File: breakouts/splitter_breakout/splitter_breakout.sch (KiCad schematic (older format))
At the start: 8 parts

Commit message: added breakout boards
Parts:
- removed H? (x4): MOUNTING_HOLE, symbol MOUNTING_HOLE
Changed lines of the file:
@@
 LIBS:scbd-16-63
 LIBS:tcm-63ax+
+LIBS:splitter_breakout-cache
 EELAYER 25 0
 EELAYER END
@@
 	8600 4200 9150 4200
 $Comp
-L MOUNTING_HOLE H?
-U 1 1 56A5DF97
-P 6300 2750
-F 0 "H?" H 6000 2800 60  0000 C CNN
-F 1 "MOUNTING_HOLE" H 6300 2900 60  0000 C CNN
-F 2 "" H 6300 2750 60  0000 C CNN
-F 3 "" H 6300 2750 60  0000 C CNN
-	1    6300 2750
-	1    0    0    -1
-$EndComp
-$Comp
-L MOUNTING_HOLE H?
-U 1 1 56A5DFB9
-P 6550 2750
-F 0 "H?" H 6250 2800 60  0000 C CNN
-F 1 "MOUNTING_HOLE" H 6550 2900 60  0000 C CNN
-F 2 "" H 6550 2750 60  0000 C CNN
-F 3 "" H 6550 2750 60  0000 C CNN
-	1    6550 2750
-	1    0    0    -1
-$EndComp
-$Comp
-L MOUNTING_HOLE H?
-U 1 1 56A5DFE1
-P 6800 2750
-F 0 "H?" H 6500 2800 60  0000 C CNN
-F 1 "MOUNTING_HOLE" H 6800 2900 60  0000 C CNN
-F 2 "" H 6800 2750 60  0000 C CNN
-F 3 "" H 6800 2750 60  0000 C CNN
-	1    6800 2750
-	1    0    0    -1
-$EndComp
-$Comp
-L MOUNTING_HOLE H?
-U 1 1 56A5E033
-P 7050 2750
-F 0 "H?" H 6750 2800 60  0000 C CNN
-F 1 "MOUNTING_HOLE" H 7050 2900 60  0000 C CNN
-F 2 "" H 7050 2750 60  0000 C CNN
-F 3 "" H 7050 2750 60  0000 C CNN
-	1    7050 2750
-	1    0    0    -1
-$EndComp
-$Comp
 L GND #PWR?

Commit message: work on breakouts
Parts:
- added U2: mounting_box, vna_footprints:POMONA_2400BOX, symbol mounting_box
- U1, U4, U5: renamed from U?; footprint (none) -> vna_footprints:732512200_SMA
- U3: renamed from U?; footprint (none) -> vna_footprints:FV1206
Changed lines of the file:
@@
 LIBS:scbd-16-63
 LIBS:tcm-63ax+
+LIBS:mounting_box
 LIBS:splitter_breakout-cache
 EELAYER 25 0
@@
 $EndDescr
 $Comp
-L PWR_SPLITTER U?
+L PWR_SPLITTER U3
 U 1 1 56A5DB75
 P 7650 3800
-F 0 "U?" H 7250 4200 60  0000 C CNN
+F 0 "U3" H 7250 4200 60  0000 C CNN
 F 1 "PWR_SPLITTER" H 7500 4300 60  0000 C CNN
-F 2 "" H 7650 3800 60  0000 C CNN
+F 2 "vna_footprints:FV1206" H 7650 3800 60  0001 C CNN
 F 3 "" H 7650 3800 60  0000 C CNN
 	1    7650 3800
@@
 $EndComp
 $Comp
-L CONN_SMA U?
+L CONN_SMA U5
 U 1 1 56A5DD34
 P 9700 4200
-F 0 "U?" H 9350 4400 60  0000 C CNN
+F 0 "U5" H 9350 4400 60  0000 C CNN
 F 1 "CONN_SMA" H 9550 4550 60  0000 C CNN
-F 2 "" H 9700 4200 60  0000 C CNN
+F 2 "vna_footprints:732512200_SMA" H 9700 4200 60  0001 C CNN
 F 3 "" H 9700 4200 60  0000 C CNN
 	1    9700 4200
@@
 $EndComp
 $Comp
-L CONN_SMA U?
+L CONN_SMA U4
 U 1 1 56A5DDCB
 P 9700 3350
-F 0 "U?" H 9350 3550 60  0000 C CNN
+F 0 "U4" H 9350 3550 60  0000 C CNN
 F 1 "CONN_SMA" H 9550 3700 60  0000 C CNN
-F 2 "" H 9700 3350 60  0000 C CNN
+F 2 "vna_footprints:732512200_SMA" H 9700 3350 60  0001 C CNN
 F 3 "" H 9700 3350 60  0000 C CNN
 	1    9700 3350
@@
 $EndComp
 $Comp
-L CONN_SMA U?
+L CONN_SMA U1
 U 1 1 56A5DE18
 P 6150 3800
-F 0 "U?" H 5800 4000 60  0000 C CNN
+F 0 "U1" H 5800 4000 60  0000 C CNN
 F 1 "CONN_SMA" H 6000 4150 60  0000 C CNN
-F 2 "" H 6150 3800 60  0000 C CNN
+F 2 "vna_footprints:732512200_SMA" H 6150 3800 60  0001 C CNN
 F 3 "" H 6150 3800 60  0000 C CNN
 	1    6150 3800
@@
 	8600 4200 9150 4200
 $Comp
-L GND #PWR?
+L GND #PWR01
 U 1 1 56A5E0B0
 P 6150 4350
-F 0 "#PWR?" H 6150 4100 50  0001 C CNN
+F 0 "#PWR01" H 6150 4100 50  0001 C CNN
 F 1 "GND" H 6150 4200 50  0000 C CNN
 F 2 "" H 6150 4350 60  0000 C CNN
@@
 Connection ~ 6100 4300
 $Comp
-L GND #PWR?
+L GND #PWR02
 U 1 1 56A5E19A
 P 9700 4750
-F 0 "#PWR?" H 9700 4500 50  0001 C CNN
+F 0 "#PWR02" H 9700 4500 50  0001 C CNN
 F 1 "GND" H 9700 4600 50  0000 C CNN
 F 2 "" H 9700 4750 60  0000 C CNN
@@
 Connection ~ 9650 4700
 $Comp
-L GND #PWR?
+L GND #PWR03
 U 1 1 56A5E1BB
 P 9700 3900
-F 0 "#PWR?" H 9700 3650 50  0001 C CNN
+F 0 "#PWR03" H 9700 3650 50  0001 C CNN
 F 1 "GND" H 9700 3750 50  0000 C CNN
 F 2 "" H 9700 3900 60  0000 C CNN
@@
 	9650 3800 9650 3850
 Connection ~ 9650 3850
+$Comp
+L mounting_box U2
+U 1 1 56B557EC
+P 7600 5000
+F 0 "U2" H 7600 5000 60  0000 C CNN
+F 1 "mounting_box" H 7550 5150 60  0000 C CNN
+F 2 "vna_footprints:POMONA_2400BOX" H 7600 5000 60  0001 C CNN
+F 3 "" H 7600 5000 60  0000 C CNN
+	1    7600 5000
+	1    0    0    -1
+$EndComp
 $EndSCHEMATC

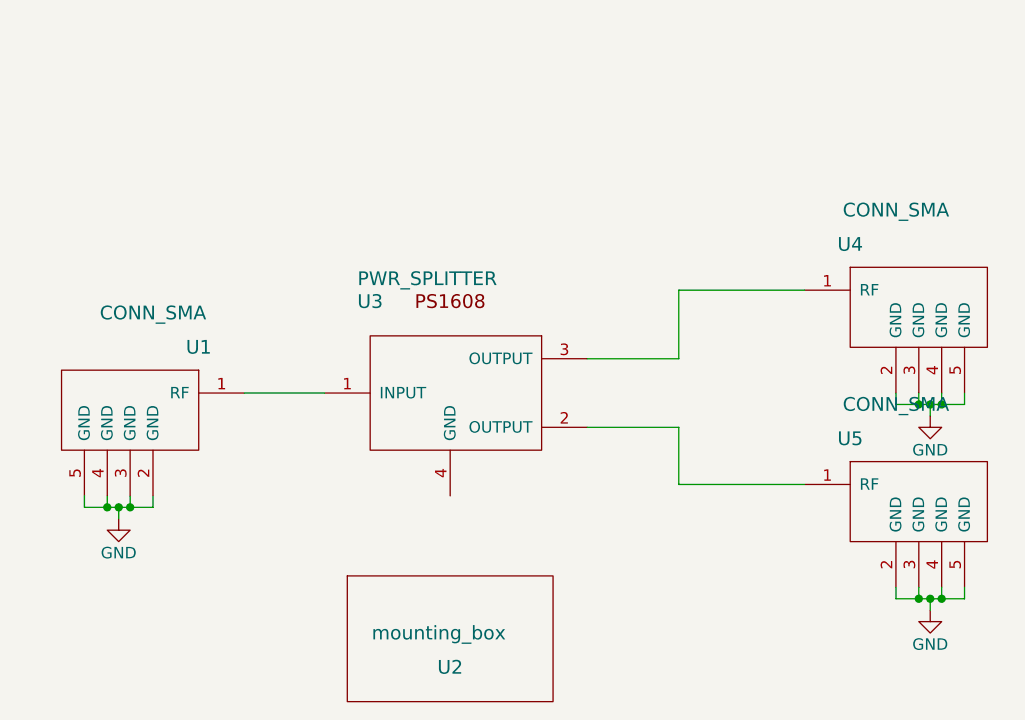
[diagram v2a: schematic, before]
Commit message: layout of splitter, switch, and filter
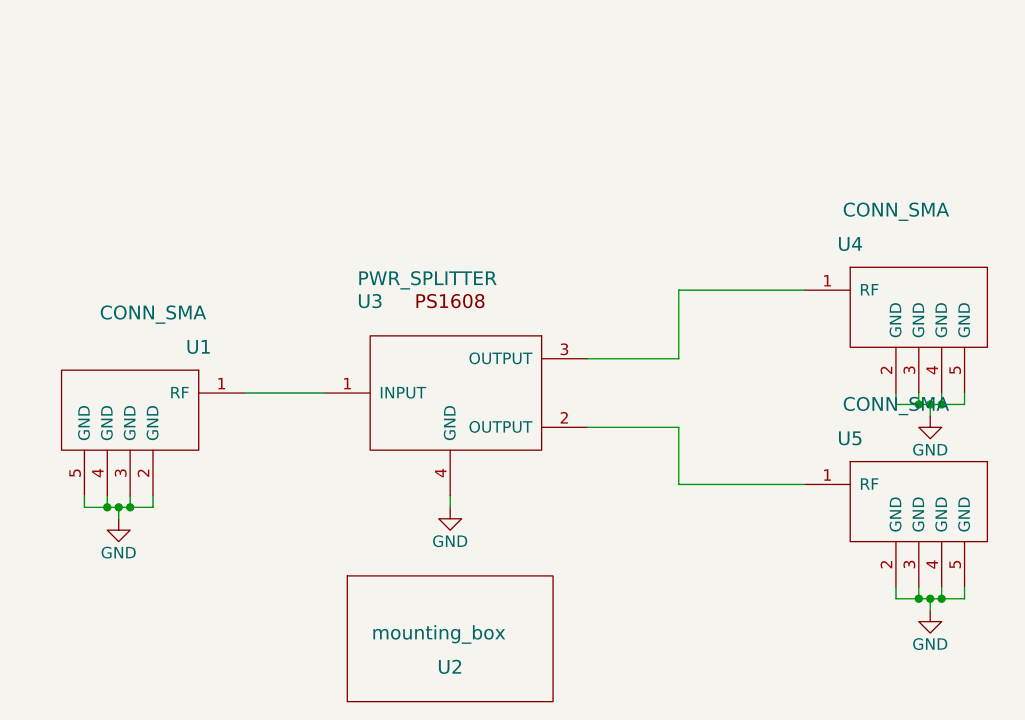
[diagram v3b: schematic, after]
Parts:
- U3: footprint vna_footprints:FV1206 -> vna_footprints:PS1608
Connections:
- net GND: now also U3.4 (GND)
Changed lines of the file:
@@
 F 0 "U3" H 7250 4200 60  0000 C CNN
 F 1 "PWR_SPLITTER" H 7500 4300 60  0000 C CNN
-F 2 "vna_footprints:FV1206" H 7650 3800 60  0001 C CNN
+F 2 "vna_footprints:PS1608" H 7650 3800 60  0001 C CNN
 F 3 "" H 7650 3800 60  0000 C CNN
 	1    7650 3800
@@
 	1    0    0    -1
 $EndComp
+$Comp
+L GND #PWR04
+U 1 1 56CE4FC7
+P 7600 4300
+F 0 "#PWR04" H 7600 4050 50  0001 C CNN
+F 1 "GND" H 7600 4150 50  0000 C CNN
+F 2 "" H 7600 4300 60  0000 C CNN
+F 3 "" H 7600 4300 60  0000 C CNN
+	1    7600 4300
+	1    0    0    -1
+$EndComp
+Wire Wire Line
+	7600 4250 7600 4300
 $EndSCHEMATC

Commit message: trimmed ground plane on some breakouts so it doesn't disappear during panelization..
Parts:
- U1, U4, U5: footprint vna_footprints:732512200_SMA -> vna_footprints:732511150_sma
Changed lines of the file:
@@
 F 0 "U5" H 9350 4400 60  0000 C CNN
 F 1 "CONN_SMA" H 9550 4550 60  0000 C CNN
-F 2 "vna_footprints:732512200_SMA" H 9700 4200 60  0001 C CNN
+F 2 "vna_footprints:732511150_sma" H 9700 4200 60  0001 C CNN
 F 3 "" H 9700 4200 60  0000 C CNN
 	1    9700 4200
@@
 F 0 "U4" H 9350 3550 60  0000 C CNN
 F 1 "CONN_SMA" H 9550 3700 60  0000 C CNN
-F 2 "vna_footprints:732512200_SMA" H 9700 3350 60  0001 C CNN
+F 2 "vna_footprints:732511150_sma" H 9700 3350 60  0001 C CNN
 F 3 "" H 9700 3350 60  0000 C CNN
 	1    9700 3350
@@
 F 0 "U1" H 5800 4000 60  0000 C CNN
 F 1 "CONN_SMA" H 6000 4150 60  0000 C CNN
-F 2 "vna_footprints:732512200_SMA" H 6150 3800 60  0001 C CNN
+F 2 "vna_footprints:732511150_sma" H 6150 3800 60  0001 C CNN
 F 3 "" H 6150 3800 60  0000 C CNN
 	1    6150 3800

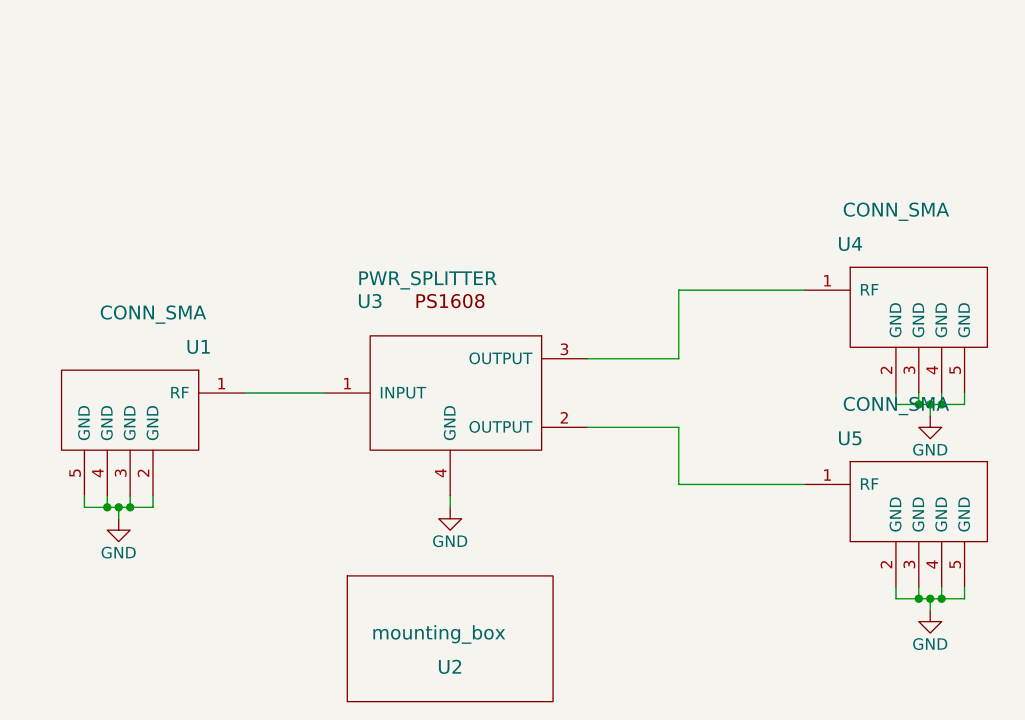
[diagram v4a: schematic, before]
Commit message: finished bias module, modified mixer, splitter, and switch sma connector footprints
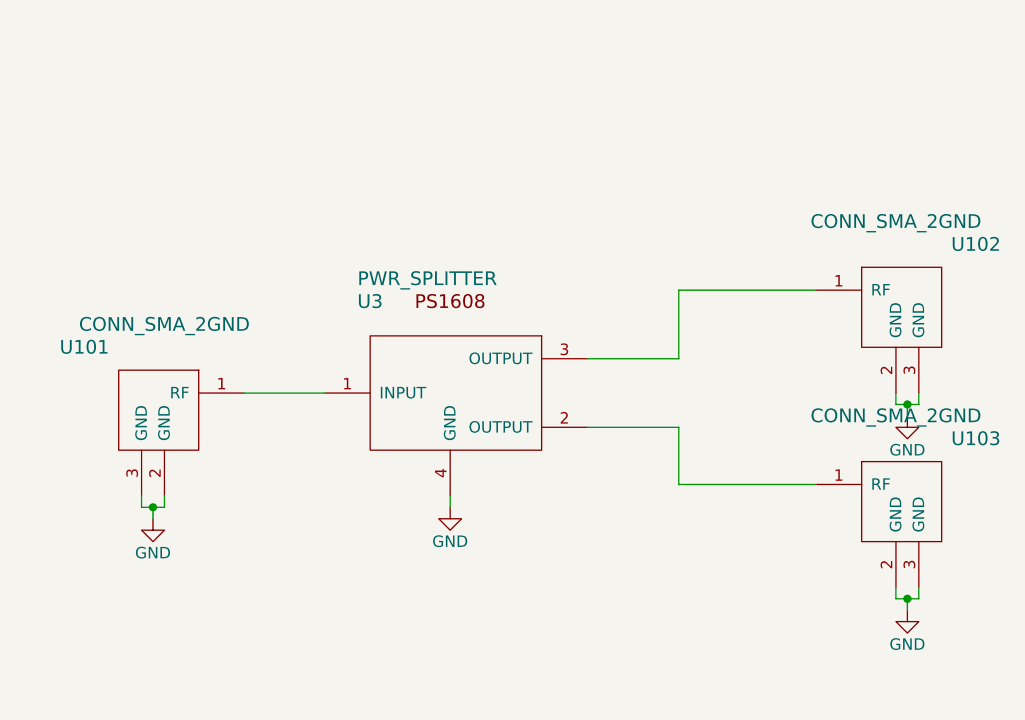
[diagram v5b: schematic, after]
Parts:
- removed U1, U4, U5: CONN_SMA, vna_footprints:732511150_sma, symbol CONN_SMA
- removed U2: mounting_box, vna_footprints:POMONA_2400BOX, symbol mounting_box
- added U101, U102, U103: CONN_SMA_2GND, vna_footprints:142-0721-882_sma_cutout, symbol CONN_SMA_2GND
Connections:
- net GND: now also U101.2 (GND), U101.3 (GND), U102.2 (GND), U102.3 (GND), U103.2 (GND), U103.3 (GND)
- net at U3.1 (INPUT): now also U101.1 (RF)
- net at U3.2 (OUTPUT): now also U103.1 (RF)
- net at U3.3 (OUTPUT): now also U102.1 (RF)
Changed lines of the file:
@@
 LIBS:tcm-63ax+
 LIBS:mounting_box
+LIBS:conn_sma_2gnd
 LIBS:splitter_breakout-cache
 EELAYER 25 0
@@
 	1    0    0    -1
 $EndComp
-$Comp
-L CONN_SMA U5
-U 1 1 56A5DD34
-P 9700 4200
-F 0 "U5" H 9350 4400 60  0000 C CNN
-F 1 "CONN_SMA" H 9550 4550 60  0000 C CNN
-F 2 "vna_footprints:732511150_sma" H 9700 4200 60  0001 C CNN
-F 3 "" H 9700 4200 60  0000 C CNN
-	1    9700 4200
-	1    0    0    -1
-$EndComp
-$Comp
-L CONN_SMA U4
-U 1 1 56A5DDCB
-P 9700 3350
-F 0 "U4" H 9350 3550 60  0000 C CNN
-F 1 "CONN_SMA" H 9550 3700 60  0000 C CNN
-F 2 "vna_footprints:732511150_sma" H 9700 3350 60  0001 C CNN
-F 3 "" H 9700 3350 60  0000 C CNN
-	1    9700 3350
-	1    0    0    -1
-$EndComp
-$Comp
-L CONN_SMA U1
-U 1 1 56A5DE18
-P 6150 3800
-F 0 "U1" H 5800 4000 60  0000 C CNN
-F 1 "CONN_SMA" H 6000 4150 60  0000 C CNN
-F 2 "vna_footprints:732511150_sma" H 6150 3800 60  0001 C CNN
-F 3 "" H 6150 3800 60  0000 C CNN
-	1    6150 3800
-	-1   0    0    -1
-$EndComp
 Wire Wire Line
 	6700 3800 7050 3800
 Wire Wire Line
-	9150 3350 8600 3350
+	8600 3350 9200 3350
 Wire Wire Line
 	8600 3350 8600 3650
@@
 	8600 3950 8600 4200
 Wire Wire Line
-	8600 4200 9150 4200
+	8600 4200 9200 4200
 $Comp
 L GND #PWR01
 U 1 1 56A5E0B0
-P 6150 4350
-F 0 "#PWR01" H 6150 4100 50  0001 C CNN
-F 1 "GND" H 6150 4200 50  0000 C CNN
-F 2 "" H 6150 4350 60  0000 C CNN
-F 3 "" H 6150 4350 60  0000 C CNN
-	1    6150 4350
-	1    0    0    -1
-$EndComp
-Wire Wire Line
-	6150 4350 6150 4300
-Wire Wire Line
-	6000 4300 6300 4300
-Wire Wire Line
-	6000 4300 6000 4250
-Wire Wire Line
-	6300 4300 6300 4250
-Connection ~ 6150 4300
-Wire Wire Line
-	6200 4250 6200 4300
-Connection ~ 6200 4300
-Wire Wire Line
-	6100 4250 6100 4300
-Connection ~ 6100 4300
-$Comp
-L GND #PWR02
-U 1 1 56A5E19A
-P 9700 4750
-F 0 "#PWR02" H 9700 4500 50  0001 C CNN
-F 1 "GND" H 9700 4600 50  0000 C CNN
-F 2 "" H 9700 4750 60  0000 C CNN
-F 3 "" H 9700 4750 60  0000 C CNN
-	1    9700 4750
-	1    0    0    -1
-$EndComp
-Wire Wire Line
-	9700 4750 9700 4700
-Wire Wire Line
-	9550 4700 9850 4700
-Wire Wire Line
-	9550 4700 9550 4650
-Wire Wire Line
-	9850 4700 9850 4650
-Connection ~ 9700 4700
-Wire Wire Line
-	9750 4650 9750 4700
-Connection ~ 9750 4700
-Wire Wire Line
-	9650 4650 9650 4700
-Connection ~ 9650 4700
-$Comp
-L GND #PWR03
-U 1 1 56A5E1BB
-P 9700 3900
-F 0 "#PWR03" H 9700 3650 50  0001 C CNN
-F 1 "GND" H 9700 3750 50  0000 C CNN
-F 2 "" H 9700 3900 60  0000 C CNN
-F 3 "" H 9700 3900 60  0000 C CNN
-	1    9700 3900
-	1    0    0    -1
-$EndComp
-Wire Wire Line
-	9700 3900 9700 3850
-Wire Wire Line
-	9550 3850 9850 3850
-Wire Wire Line
-	9550 3850 9550 3800
-Wire Wire Line
-	9850 3850 9850 3800
-Connection ~ 9700 3850
-Wire Wire Line
-	9750 3800 9750 3850
-Connection ~ 9750 3850
-Wire Wire Line
-	9650 3800 9650 3850
-Connection ~ 9650 3850
-$Comp
-L mounting_box U2
-U 1 1 56B557EC
-P 7600 5000
-F 0 "U2" H 7600 5000 60  0000 C CNN
-F 1 "mounting_box" H 7550 5150 60  0000 C CNN
-F 2 "vna_footprints:POMONA_2400BOX" H 7600 5000 60  0001 C CNN
-F 3 "" H 7600 5000 60  0000 C CNN
-	1    7600 5000
+P 6300 4350
+F 0 "#PWR01" H 6300 4100 50  0001 C CNN
+F 1 "GND" H 6300 4200 50  0000 C CNN
+F 2 "" H 6300 4350 60  0000 C CNN
+F 3 "" H 6300 4350 60  0000 C CNN
+	1    6300 4350
 	1    0    0    -1
 $EndComp
 $Comp
-L GND #PWR04
+L GND #PWR02
 U 1 1 56CE4FC7
 P 7600 4300
-F 0 "#PWR04" H 7600 4050 50  0001 C CNN
+F 0 "#PWR02" H 7600 4050 50  0001 C CNN
 F 1 "GND" H 7600 4150 50  0000 C CNN
 F 2 "" H 7600 4300 60  0000 C CNN
@@
 Wire Wire Line
 	7600 4250 7600 4300
+$Comp
+L CONN_SMA_2GND U101
+U 1 1 576CD210
+P 6300 3800
+F 0 "U101" H 6000 4000 60  0000 C CNN
+F 1 "CONN_SMA_2GND" H 6350 4100 60  0000 C CNN
+F 2 "vna_footprints:142-0721-882_sma_cutout" H 6300 3800 60  0001 C CNN
+F 3 "" H 6300 3800 60  0000 C CNN
+	1    6300 3800
+	1    0    0    -1
+$EndComp
+Wire Wire Line
+	6250 4250 6250 4300
+Wire Wire Line
+	6250 4300 6350 4300
+Wire Wire Line
+	6350 4300 6350 4250
+Wire Wire Line
+	6300 4300 6300 4350
+Connection ~ 6300 4300
+$Comp
+L GND #PWR03
+U 1 1 576CD392
+P 9600 4750
+F 0 "#PWR03" H 9600 4500 50  0001 C CNN
+F 1 "GND" H 9600 4600 50  0000 C CNN
+F 2 "" H 9600 4750 60  0000 C CNN
+F 3 "" H 9600 4750 60  0000 C CNN
+	1    9600 4750
+	-1   0    0    -1
+$EndComp
+$Comp
+L CONN_SMA_2GND U103
+U 1 1 576CD398
+P 9600 4200
+F 0 "U103" H 9300 4400 60  0000 C CNN
+F 1 "CONN_SMA_2GND" H 9650 4500 60  0000 C CNN
+F 2 "vna_footprints:142-0721-882_sma_cutout" H 9600 4200 60  0001 C CNN
+F 3 "" H 9600 4200 60  0000 C CNN
+	1    9600 4200
+	-1   0    0    -1
+$EndComp
+Wire Wire Line
+	9650 4650 9650 4700
+Wire Wire Line
+	9650 4700 9550 4700
+Wire Wire Line
+	9550 4700 9550 4650
+Wire Wire Line
+	9600 4700 9600 4750
+Connection ~ 9600 4700
+$Comp
+L GND #PWR04
+U 1 1 576CD427
+P 9600 3900
+F 0 "#PWR04" H 9600 3650 50  0001 C CNN
+F 1 "GND" H 9600 3750 50  0000 C CNN
+F 2 "" H 9600 3900 60  0000 C CNN
+F 3 "" H 9600 3900 60  0000 C CNN
+	1    9600 3900
+	-1   0    0    -1
+$EndComp
+$Comp
+L CONN_SMA_2GND U102
+U 1 1 576CD42D
+P 9600 3350
+F 0 "U102" H 9300 3550 60  0000 C CNN
+F 1 "CONN_SMA_2GND" H 9650 3650 60  0000 C CNN
+F 2 "vna_footprints:142-0721-882_sma_cutout" H 9600 3350 60  0001 C CNN
+F 3 "" H 9600 3350 60  0000 C CNN
+	1    9600 3350
+	-1   0    0    -1
+$EndComp
+Wire Wire Line
+	9650 3800 9650 3850
+Wire Wire Line
+	9650 3850 9550 3850
+Wire Wire Line
+	9550 3850 9550 3800
+Wire Wire Line
+	9600 3850 9600 3900
+Connection ~ 9600 3850
 $EndSCHEMATC
